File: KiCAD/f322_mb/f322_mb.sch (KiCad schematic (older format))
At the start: 13 parts, among them Q1 2N3904, SW1 power, SW2 play, U1 PIC10(L)F322-I_P

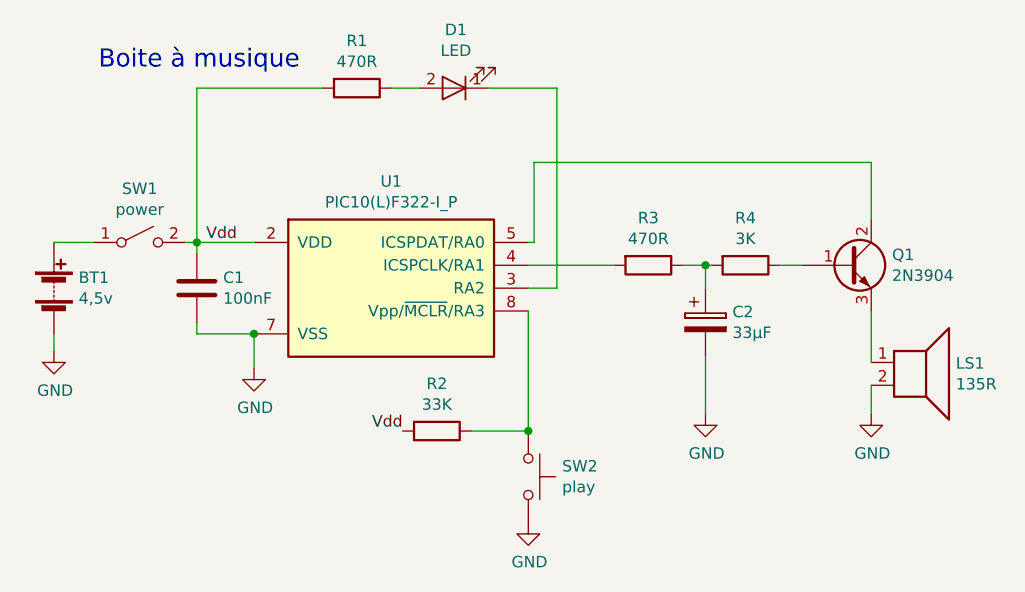
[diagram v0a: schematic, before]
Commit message: travail sur version pic10f322 de la boite à musique
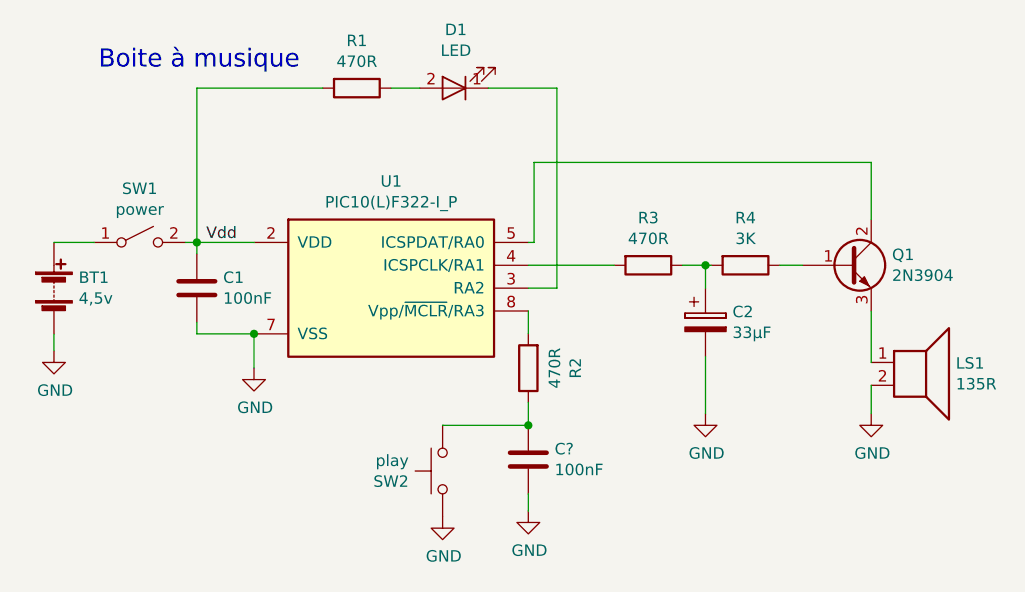
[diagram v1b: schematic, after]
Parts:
- added C?: 100nF, symbol device:C
- R2: value 33K -> 470R
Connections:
- net GND: now also SW2.1, C?.2; no longer SW2.2
- net Vdd: no longer R2.2
- new net: R2.2, U1.8 (Vpp/~MCLR~/RA3)
- new net: C?.1, R2.1, SW2.2
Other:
- moved on the sheet: R2, SW2
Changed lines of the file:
@@
 EESchema Schematic File Version 4
+LIBS:f322_mb-cache
 EELAYER 26 0
 EELAYER END
@@
 L switches:SW_Push SW2
 U 1 1 5C01F097
-P 5950 4475
-F 0 "SW2" V 5904 4623 50  0000 L CNN
-F 1 "play" V 5995 4623 50  0000 L CNN
-F 2 "" H 5950 4675 50  0001 C CNN
-F 3 "" H 5950 4675 50  0001 C CNN
-	1    5950 4475
-	0    1    1    0
+P 5575 4450
+F 0 "SW2" V 5529 4598 50  0000 L CNN
+F 1 "play" V 5620 4598 50  0000 L CNN
+F 2 "" H 5575 4650 50  0001 C CNN
+F 3 "" H 5575 4650 50  0001 C CNN
+	1    5575 4450
+	0    -1   -1   0
 $EndComp
 $Comp
 L device:R R2
 U 1 1 5C01F0F9
-P 5550 4275
-F 0 "R2" V 5343 4275 50  0000 C CNN
-F 1 "33K" V 5434 4275 50  0000 C CNN
-F 2 "" V 5480 4275 50  0001 C CNN
-F 3 "" H 5550 4275 50  0001 C CNN
-	1    5550 4275
-	0    1    1    0
+P 5950 4000
+F 0 "R2" V 5743 4000 50  0000 C CNN
+F 1 "470R" V 5834 4000 50  0000 C CNN
+F 2 "" V 5880 4000 50  0001 C CNN
+F 3 "" H 5950 4000 50  0001 C CNN
+	1    5950 4000
+	-1   0    0    1
 $EndComp
 $Comp
@@
 Wire Wire Line
 	6075 3650 5950 3650
-Wire Wire Line
-	5950 3750 5950 4275
 $Comp
 L power:GND #PWR03
 U 1 1 5C0202E9
-P 5950 4675
-F 0 "#PWR03" H 5950 4425 50  0001 C CNN
-F 1 "GND" H 5955 4502 50  0000 C CNN
-F 2 "" H 5950 4675 50  0001 C CNN
-F 3 "" H 5950 4675 50  0001 C CNN
-	1    5950 4675
-	1    0    0    -1
-$EndComp
-Wire Wire Line
-	5700 4275 5950 4275
-Connection ~ 5950 4275
+P 5575 4650
+F 0 "#PWR03" H 5575 4400 50  0001 C CNN
+F 1 "GND" H 5580 4477 50  0000 C CNN
+F 2 "" H 5575 4650 50  0001 C CNN
+F 3 "" H 5575 4650 50  0001 C CNN
+	1    5575 4650
+	1    0    0    -1
+$EndComp
 Wire Wire Line
 	3875 3450 4050 3450
@@
 Wire Wire Line
 	4500 2775 5050 2775
-Text Label 5400 4275 2    50   ~ 0
-Vdd
 Text Label 4675 3450 2    50   ~ 0
 Vdd
 Text Notes 4950 2700 2    79   ~ 0
 Boite à musique
+$Comp
+L device:C C?
+U 1 1 5C034586
+P 5950 4400
+F 0 "C?" H 6065 4446 50  0000 L CNN
+F 1 "100nF" H 6065 4355 50  0000 L CNN
+F 2 "" H 5988 4250 50  0001 C CNN
+F 3 "" H 5950 4400 50  0001 C CNN
+	1    5950 4400
+	1    0    0    -1
+$EndComp
+$Comp
+L power:GND #PWR?
+U 1 1 5C034630
+P 5950 4625
+F 0 "#PWR?" H 5950 4375 50  0001 C CNN
+F 1 "GND" H 5955 4452 50  0000 C CNN
+F 2 "" H 5950 4625 50  0001 C CNN
+F 3 "" H 5950 4625 50  0001 C CNN
+	1    5950 4625
+	1    0    0    -1
+$EndComp
+Wire Wire Line
+	5950 4550 5950 4625
+Wire Wire Line
+	5950 3750 5950 3850
+Wire Wire Line
+	5575 4250 5950 4250
+Wire Wire Line
+	5950 4250 5950 4150
+Connection ~ 5950 4250
 $EndSCHEMATC
